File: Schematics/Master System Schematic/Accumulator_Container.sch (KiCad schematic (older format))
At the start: 20 parts, among them J4 Shutdown/MC Control Connector, J5 TSMP/IMD Connector, J6 Main TS Connector, J7 TSAL Connector, K1 SPST-NO (Precharge), K2 SPST-NO (AIR), K3 SPST-NO (AIR), K4 SPST-NC (Discharge), K5 SPST-NO (Precharge Control), K6 SPST-NO (AIR Control), U5 OrionCurrentSens

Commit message: Revert "Zack BMS Edits"
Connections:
- net Shutdown+: now also J4.3; no longer J4.4
- net Shutdown-: now also J4.4; no longer J4.3
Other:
- moved on the sheet: F1, F2, F3, F8, F9, J4, J5, J6, J7, K1, K2, K3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

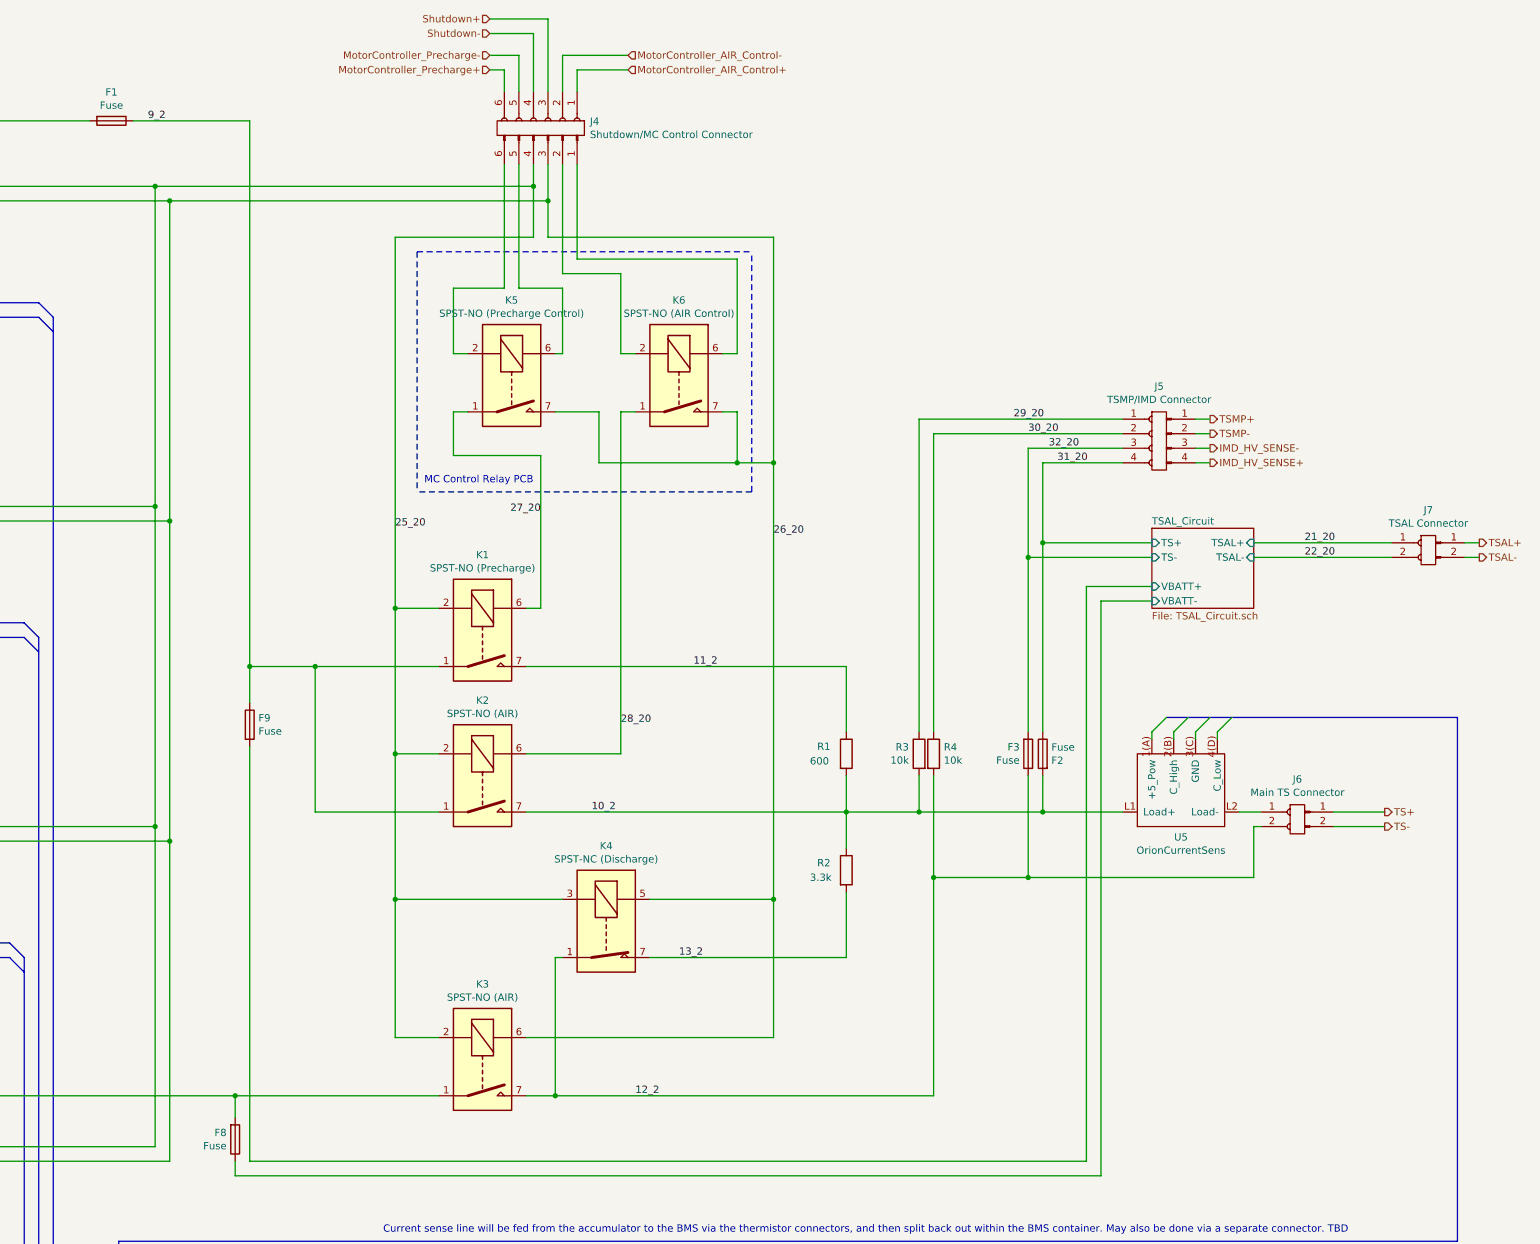
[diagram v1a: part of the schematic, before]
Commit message: Had to refactor all IDs
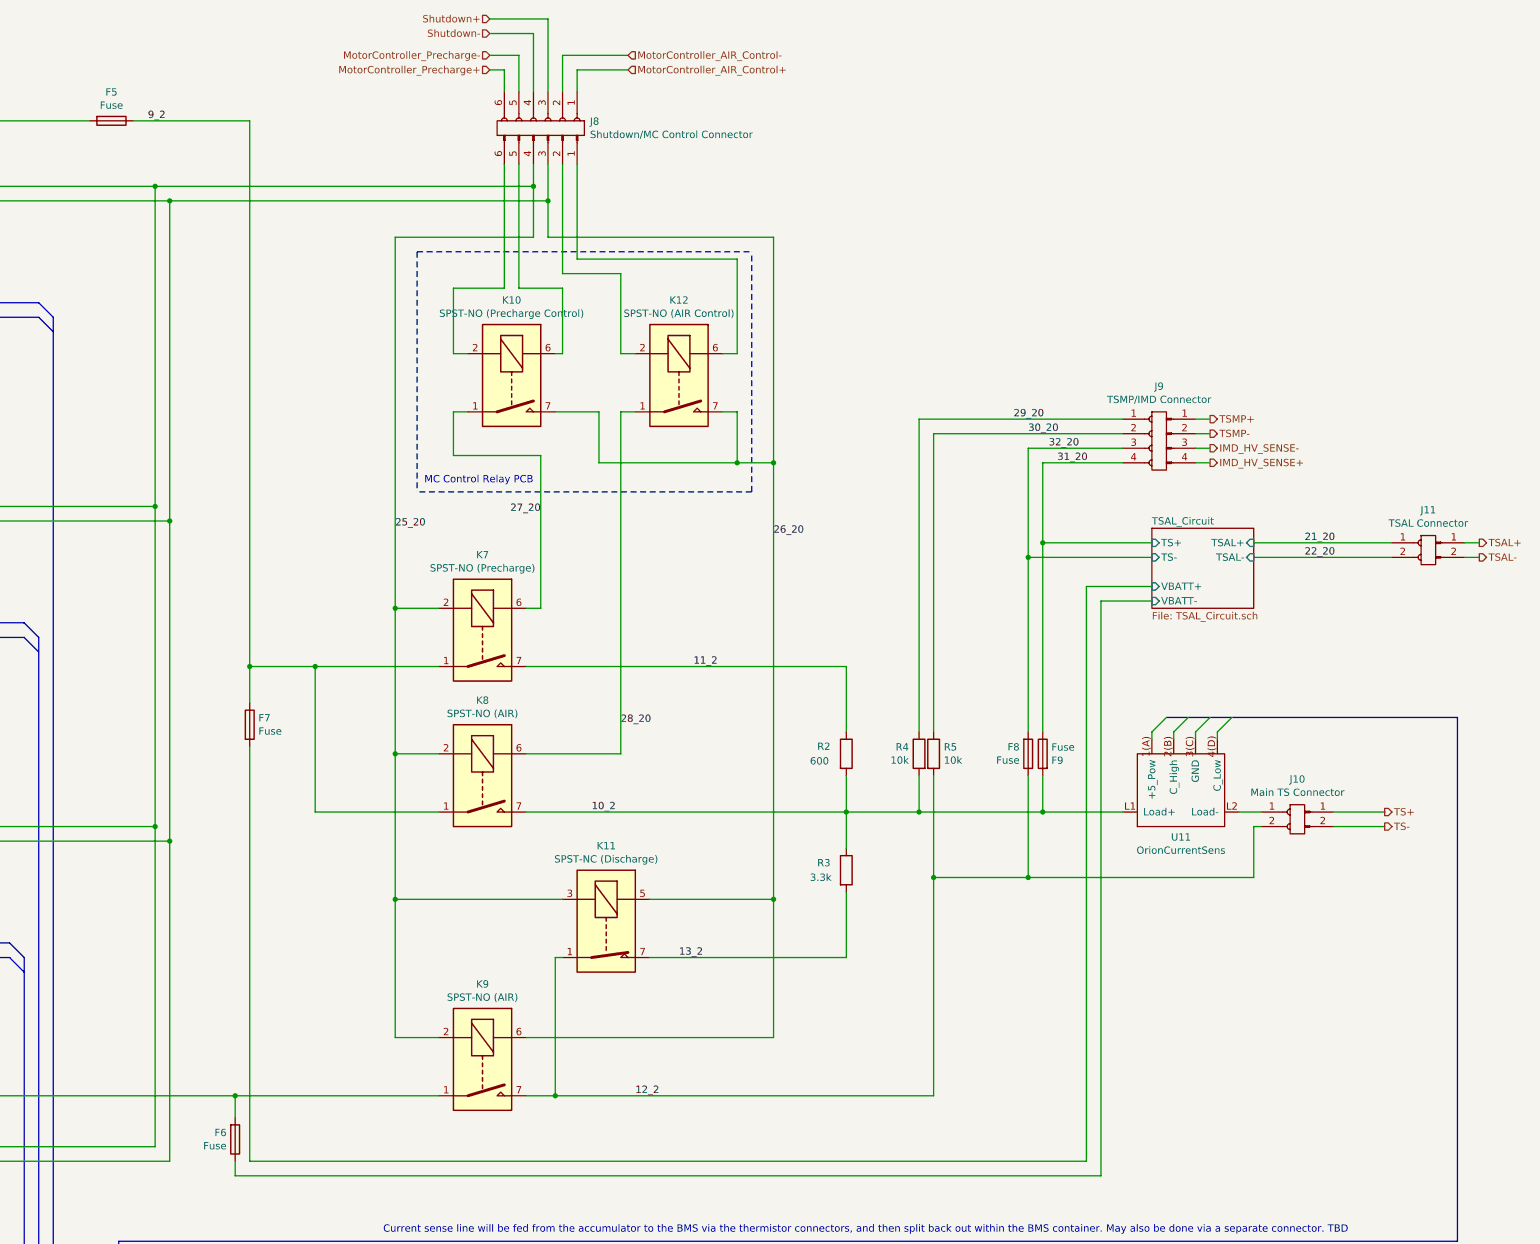
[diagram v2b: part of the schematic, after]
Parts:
- renumbered F1 to F5, F8 to F6, F9 to F7, F3 to F8, F2 to F9, J6 to J10, J7 to J11, J4 to J8, J5 to J9, K5 to K10, K4 to K11, K6 to K12, K1 to K7, K2 to K8, K3 to K9, R1 to R2, R2 to R3, R3 to R4, R4 to R5, U5 to U11
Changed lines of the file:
@@
 $Descr B 17000 11000
 encoding utf-8
-Sheet 6 21
+Sheet 7 21
 Title "Accumulator Container"
 Date "2020-10-16"
@@
 $EndDescr
 $Comp
-L Relay:MSxx-1Bxx-75 K4
+L Relay:MSxx-1Bxx-75 K11
 U 1 1 5E637554
 P 10050 6800
-F 0 "K4" V 9483 6800 50  0000 C CNN
+F 0 "K11" V 9483 6800 50  0000 C CNN
 F 1 "SPST-NC (Discharge)" V 9574 6800 50  0000 C CNN
 F 2 "Relay_THT:Relay_SPST_StandexMeder_MS_Form1AB" H 10400 6750 50  0001 L CNN
@@
 $EndComp
 $Comp
-L Device:Fuse F1
+L Device:Fuse F5
 U 1 1 5E640862
 P 6650 1250
-F 0 "F1" V 6453 1250 50  0000 C CNN
+F 0 "F5" V 6453 1250 50  0000 C CNN
 F 1 "Fuse" V 6544 1250 50  0000 C CNN
 F 2 "" V 6580 1250 50  0001 C CNN
@@
 $EndComp
 $Comp
-L Relay:DIPxx-1Axx-11x K3
+L Relay:DIPxx-1Axx-11x K9
 U 1 1 5EBDE2B9
 P 9200 7750
-F 0 "K3" V 8633 7750 50  0000 C CNN
+F 0 "K9" V 8633 7750 50  0000 C CNN
 F 1 "SPST-NO (AIR)" V 8724 7750 50  0000 C CNN
 F 2 "Relay_THT:Relay_StandexMeder_DIP_LowProfile" H 9550 7700 50  0001 L CNN
@@
 $EndComp
 $Comp
-L Relay:DIPxx-1Axx-11x K2
+L Relay:DIPxx-1Axx-11x K8
 U 1 1 5EBE5BCF
 P 9200 5800
-F 0 "K2" V 8633 5800 50  0000 C CNN
+F 0 "K8" V 8633 5800 50  0000 C CNN
 F 1 "SPST-NO (AIR)" V 8724 5800 50  0000 C CNN
 F 2 "Relay_THT:Relay_StandexMeder_DIP_LowProfile" H 9550 5750 50  0001 L CNN
@@
 $EndComp
 $Comp
-L Relay:DIPxx-1Axx-11x K1
+L Relay:DIPxx-1Axx-11x K7
 U 1 1 5EBEB71B
 P 9200 4800
-F 0 "K1" V 8633 4800 50  0000 C CNN
+F 0 "K7" V 8633 4800 50  0000 C CNN
 F 1 "SPST-NO (Precharge)" V 8724 4800 50  0000 C CNN
 F 2 "Relay_THT:Relay_StandexMeder_DIP_LowProfile" H 9550 4750 50  0001 L CNN
@@
 	9700 7000 9750 7000
 $Comp
-L Device:R R2
+L Device:R R3
 U 1 1 5F158D54
 P 11700 6400
-F 0 "R2" H 11500 6450 50  0000 L CNN
+F 0 "R3" H 11500 6450 50  0000 L CNN
 F 1 "3.3k" H 11450 6350 50  0000 L CNN
 F 2 "" V 11630 6400 50  0001 C CNN
@@
 $EndComp
 $Comp
-L Device:R R1
+L Device:R R2
 U 1 1 5F159E72
 P 11700 5600
-F 0 "R1" H 11500 5650 50  0000 L CNN
+F 0 "R2" H 11500 5650 50  0000 L CNN
 F 1 "600" H 11450 5550 50  0000 L CNN
 F 2 "" V 11630 5600 50  0001 C CNN
@@
 28_20
 $Comp
-L Device:R R3
+L Device:R R4
 U 1 1 5F2AF3BD
 P 12200 5600
-F 0 "R3" H 12270 5646 50  0000 L CNN
+F 0 "R4" H 12270 5646 50  0000 L CNN
 F 1 "10k" H 12270 5555 50  0000 L CNN
 F 2 "" V 12130 5600 50  0001 C CNN
@@
 	9750 800  9750 1050
 $Comp
-L Device:R R4
+L Device:R R5
 U 1 1 5F39A796
 P 12300 5600
-F 0 "R4" H 12370 5646 50  0000 L CNN
+F 0 "R5" H 12370 5646 50  0000 L CNN
 F 1 "10k" H 12370 5555 50  0000 L CNN
 F 2 "" V 12230 5600 50  0001 C CNN
@@
 $EndComp
 $Comp
-L Device:Fuse F2
+L Device:Fuse F9
 U 1 1 5F14BDC4
 P 13050 5600
-F 0 "F2" H 12991 5554 50  0000 R CNN
+F 0 "F9" H 12991 5554 50  0000 R CNN
 F 1 "Fuse" H 12991 5645 50  0000 R CNN
 F 2 "" V 12980 5600 50  0001 C CNN
@@
 Segment4_VoltageTaps
 $Comp
-L Device:Fuse F3
+L Device:Fuse F8
 U 1 1 5F6433FB
 P 12950 5600
-F 0 "F3" H 12891 5554 50  0000 R CNN
+F 0 "F8" H 12891 5554 50  0000 R CNN
 F 1 "Fuse" H 12891 5645 50  0000 R CNN
 F 2 "" V 12880 5600 50  0001 C CNN
@@
 	12300 3400 13600 3400
 $Comp
-L Relay:DIPxx-1Axx-11x K5
+L Relay:DIPxx-1Axx-11x K10
 U 1 1 5F80B7CF
 P 9400 3050
-F 0 "K5" V 8833 3050 50  0000 C CNN
+F 0 "K10" V 8833 3050 50  0000 C CNN
 F 1 "SPST-NO (Precharge Control)" V 8924 3050 50  0000 C CNN
 F 2 "Relay_THT:Relay_StandexMeder_DIP_LowProfile" H 9750 3000 50  0001 L CNN
@@
 MC Control Relay PCB
 $Comp
-L Relay:DIPxx-1Axx-11x K6
+L Relay:DIPxx-1Axx-11x K12
 U 1 1 5F814F76
 P 10550 3050
-F 0 "K6" V 9983 3050 50  0000 C CNN
+F 0 "K12" V 9983 3050 50  0000 C CNN
 F 1 "SPST-NO (AIR Control)" V 10074 3050 50  0000 C CNN
 F 2 "Relay_THT:Relay_StandexMeder_DIP_LowProfile" H 10900 3000 50  0001 L CNN
@@
 	10350 7000 11700 7000
 $Comp
-L NER:2-Pos_Generic J6
+L NER:2-Pos_Generic J10
 U 1 1 5F84E6B9
 P 14800 5900
-F 0 "J6" H 14800 6025 50  0000 C CNN
+F 0 "J10" H 14800 6025 50  0000 C CNN
 F 1 "Main TS Connector" H 14800 5934 50  0000 C CNN
 F 2 "" H 14800 5900 50  0001 C CNN
@@
 $EndComp
 $Comp
-L NER:4-Pos_Generic J5
+L NER:4-Pos_Generic J9
 U 1 1 5F95323D
 P 13850 3200
-F 0 "J5" H 13850 3325 50  0000 C CNN
+F 0 "J9" H 13850 3325 50  0000 C CNN
 F 1 "TSMP/IMD Connector" H 13850 3234 50  0000 C CNN
 F 2 "" H 13850 3200 50  0001 C CNN
@@
 	14100 3600 14200 3600
 $Comp
-L NER:6-Pos_Generic J4
+L NER:6-Pos_Generic J8
 U 1 1 5FAB592D
 P 9950 1300
-F 0 "J4" V 9904 1288 50  0000 L CNN
+F 0 "J8" V 9904 1288 50  0000 L CNN
 F 1 "Shutdown/MC Control Connector" V 9995 1288 50  0000 L CNN
 F 2 "" H 9950 1300 50  0001 C CNN
@@
 $EndComp
 $Comp
-L NER:OrionCurrentSens U5
+L NER:OrionCurrentSens U11
 U 1 1 5F8DBC0B
 P 14000 6150
-F 0 "U5" H 14000 6173 50  0000 C CNN
+F 0 "U11" H 14000 6173 50  0000 C CNN
 F 1 "OrionCurrentSens" H 14000 6264 50  0000 C CNN
 F 2 "" H 14000 6150 50  0001 C CNN
@@
 	15950 4150 16050 4150
 $Comp
-L NER:2-Pos_Generic J7
+L NER:2-Pos_Generic J11
 U 1 1 5F95267C
 P 15700 4050
-F 0 "J7" H 15700 4175 50  0000 C CNN
+F 0 "J11" H 15700 4175 50  0000 C CNN
 F 1 "TSAL Connector" H 15700 4084 50  0000 C CNN
 F 2 "" H 15700 4050 50  0001 C CNN
@@
 	13450 8500 7500 8500
 $Comp
-L Device:Fuse F9
+L Device:Fuse F7
 U 1 1 5FC950C3
 P 7600 5400
-F 0 "F9" H 7660 5446 50  0000 L CNN
+F 0 "F7" H 7660 5446 50  0000 L CNN
 F 1 "Fuse" H 7660 5355 50  0000 L CNN
 F 2 "" V 7530 5400 50  0001 C CNN
@@
 $EndComp
 $Comp
-L Device:Fuse F8
+L Device:Fuse F6
 U 1 1 5FC95B82
 P 7500 8250
-F 0 "F8" H 7441 8204 50  0000 R CNN
+F 0 "F6" H 7441 8204 50  0000 R CNN
 F 1 "Fuse" H 7441 8295 50  0000 R CNN
 F 2 "" V 7430 8250 50  0001 C CNN

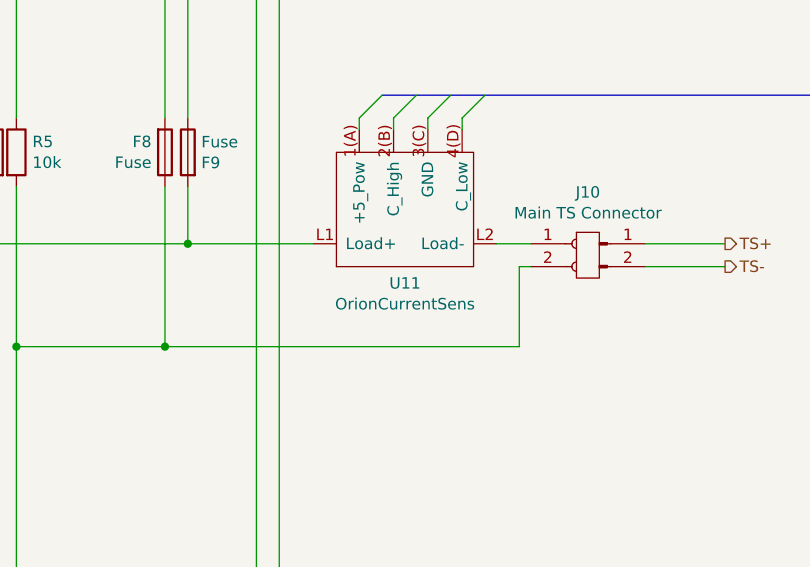
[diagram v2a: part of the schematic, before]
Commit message: Fixed Driver IO and annotations
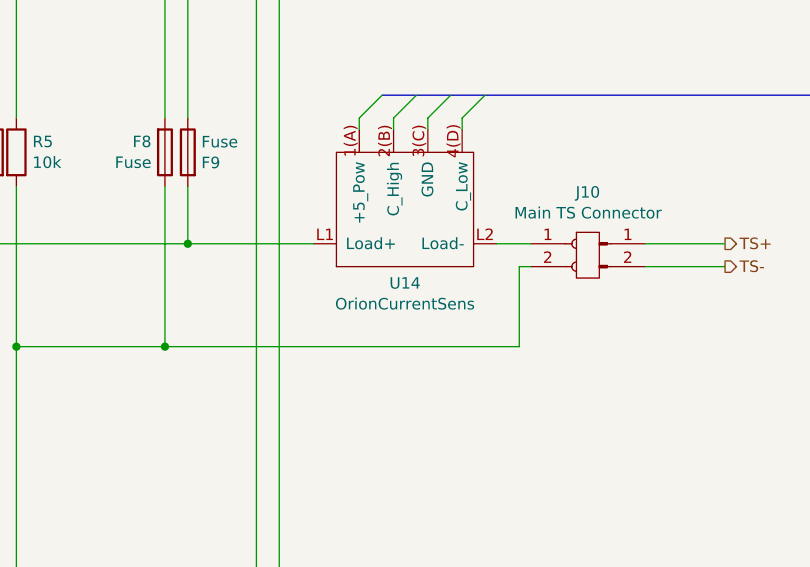
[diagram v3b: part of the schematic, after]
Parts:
- renumbered U11 to U14
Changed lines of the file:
@@
 EESchema Schematic File Version 4
-LIBS:Master System Schematic-cache
 EELAYER 30 0
 EELAYER END
@@
 $EndComp
 $Comp
-L NER:OrionCurrentSens U11
+L NER:OrionCurrentSens U14
 U 1 1 5F8DBC0B
 P 14000 6150
-F 0 "U11" H 14000 6173 50  0000 C CNN
+F 0 "U14" H 14000 6173 50  0000 C CNN
 F 1 "OrionCurrentSens" H 14000 6264 50  0000 C CNN
 F 2 "" H 14000 6150 50  0001 C CNN
